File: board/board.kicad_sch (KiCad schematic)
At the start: 4 parts, among them J1 0xx_LED, J2 0xx_LED

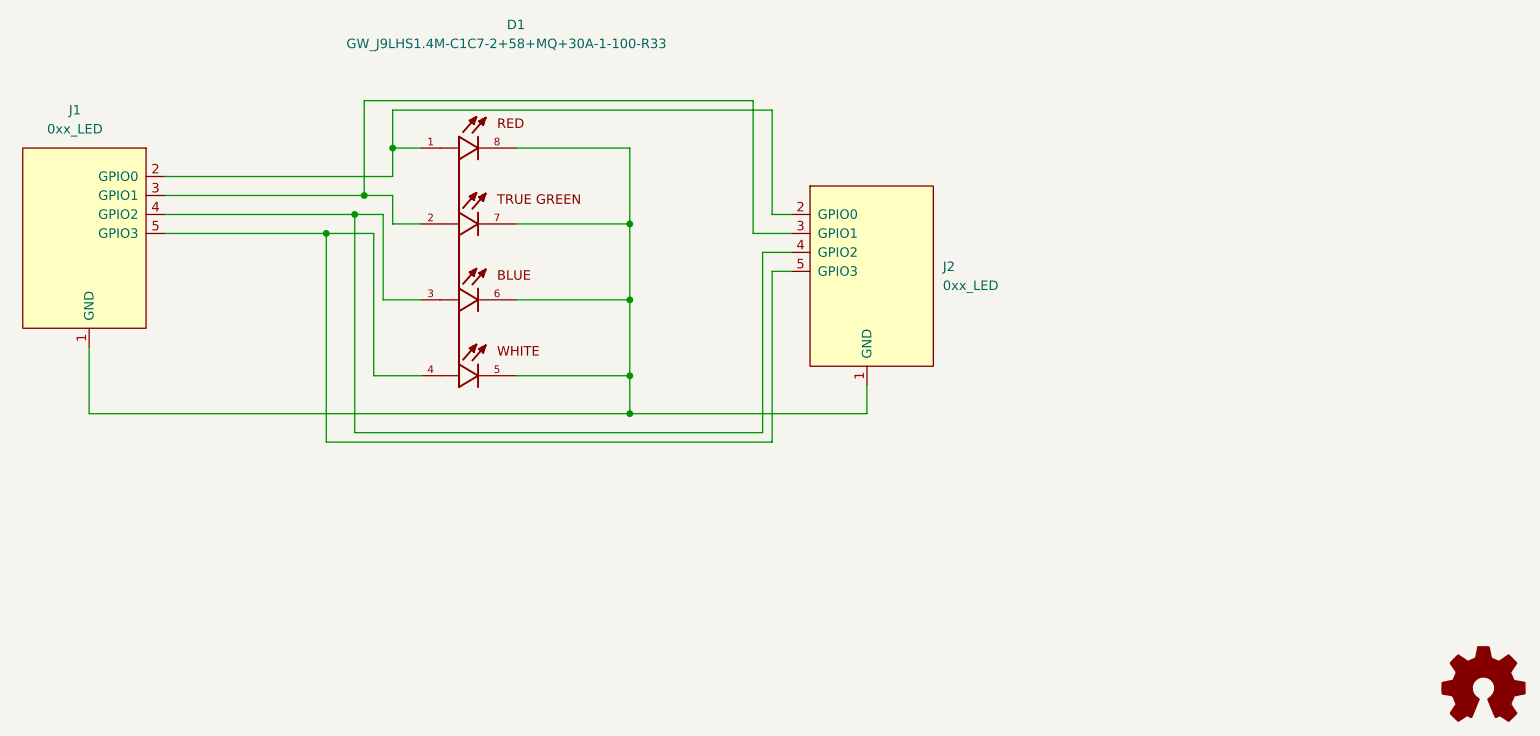
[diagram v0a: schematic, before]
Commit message: Update surface and connected vias | Change common ground to common anode
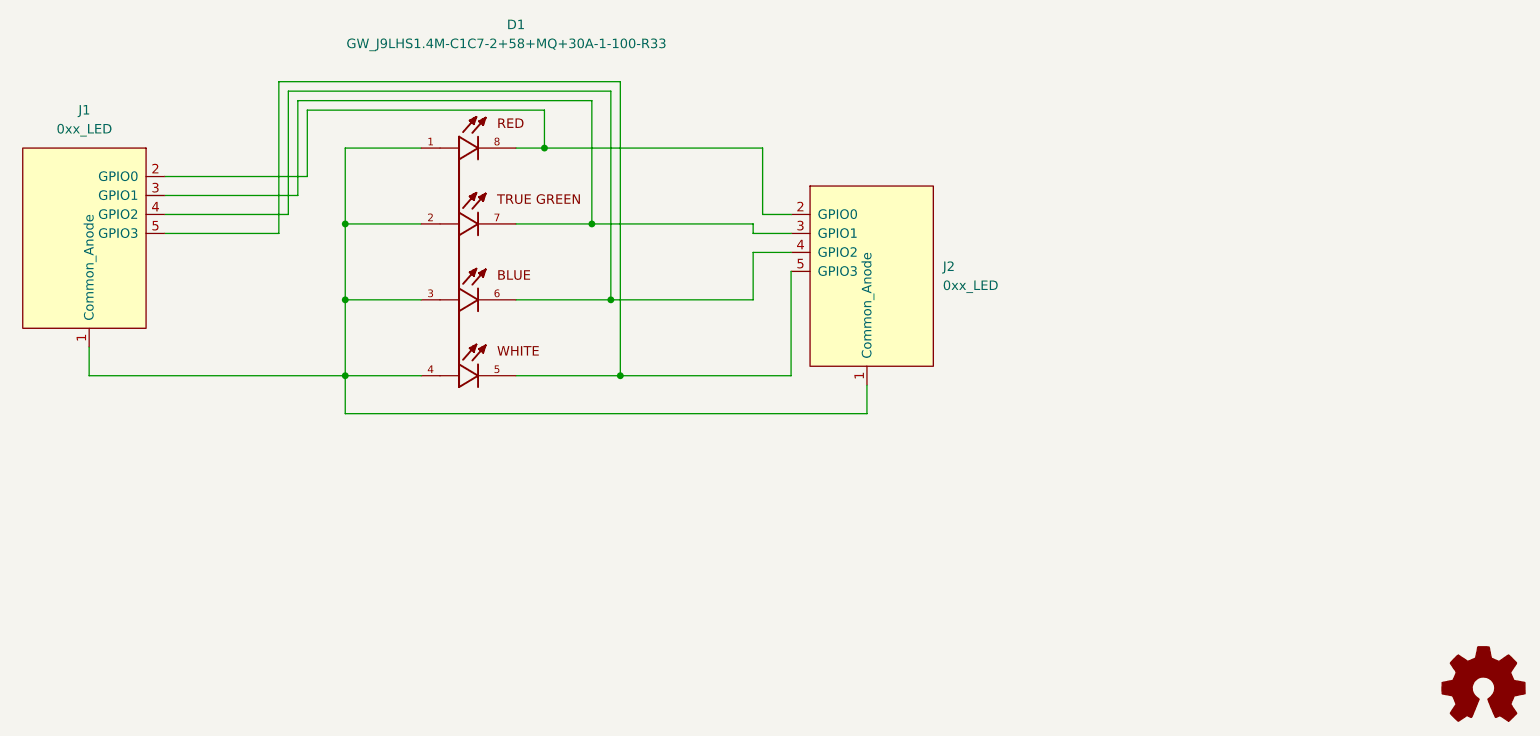
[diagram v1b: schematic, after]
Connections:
- net at J1.2 (GPIO0), J2.2 (GPIO0): now also D1.8; no longer D1.1
- net at J1.3 (GPIO1), J2.3 (GPIO1): now also D1.7; no longer D1.2
- net at J1.4 (GPIO2), J2.4 (GPIO2): now also D1.6; no longer D1.3
- net at J1.5 (GPIO3), J2.5 (GPIO3): now also D1.5; no longer D1.4
- new net: D1.1, D1.2, D1.3, D1.4, J1.1 (Common_Anode), J2.1 (Common_Anode)
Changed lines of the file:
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@@
 (kicad_sch (version 20211123) (generator eeschema)
   (paper "A4")
-  (junction (at 118.11 96.52) (diameter 0) (color 0 0 0 0)
+  (junction (at 120.65 95.25) (diameter 0) (color 0 0 0 0)
   )
-  (junction (at 158.75 95.25) (diameter 0) (color 0 0 0 0)
+  (junction (at 120.65 115.57) (diameter 0) (color 0 0 0 0)
   )
-  (junction (at 127 85.09) (diameter 0) (color 0 0 0 0)
+  (junction (at 156.21 105.41) (diameter 0) (color 0 0 0 0)
   )
-  (junction (at 158.75 105.41) (diameter 0) (color 0 0 0 0)
+  (junction (at 153.67 95.25) (diameter 0) (color 0 0 0 0)
   )
-  (junction (at 158.75 115.57) (diameter 0) (color 0 0 0 0)
+  (junction (at 147.32 85.09) (diameter 0) (color 0 0 0 0)
   )
-  (junction (at 123.19 91.44) (diameter 0) (color 0 0 0 0)
+  (junction (at 120.65 105.41) (diameter 0) (color 0 0 0 0)
   )
-  (junction (at 158.75 120.65) (diameter 0) (color 0 0 0 0)
+  (junction (at 157.48 115.57) (diameter 0) (color 0 0 0 0)
   )
-  (junction (at 121.92 93.98) (diameter 0) (color 0 0 0 0)
-  )
-  (wire (pts (xy 123.19 78.74) (xy 175.26 78.74))
+  (wire (pts (xy 86.36 115.57) (xy 120.65 115.57))
     (stroke (width 0) (type default) (color 0 0 0 0))
   )
-  (wire (pts (xy 123.19 91.44) (xy 127 91.44))
+  (wire (pts (xy 143.51 85.09) (xy 147.32 85.09))
     (stroke (width 0) (type default) (color 0 0 0 0))
   )
-  (wire (pts (xy 127 80.01) (xy 177.8 80.01))
+  (wire (pts (xy 147.32 85.09) (xy 147.32 80.01))
     (stroke (width 0) (type default) (color 0 0 0 0))
   )
-  (wire (pts (xy 118.11 96.52) (xy 96.52 96.52))
-    (stroke (width 0) (type default) (color 0 0 0 0))
-  )
-  (wire (pts (xy 96.52 93.98) (xy 121.92 93.98))
-    (stroke (width 0) (type default) (color 0 0 0 0))
-  )
-  (wire (pts (xy 127 85.09) (xy 127 80.01))
-    (stroke (width 0) (type default) (color 0 0 0 0))
-  )
-  (wire (pts (xy 158.75 95.25) (xy 143.51 95.25))
+  (wire (pts (xy 120.65 105.41) (xy 120.65 115.57))
     (stroke (width 0) (type default) (color 0 0 0 0))
   )
@@
     (stroke (width 0) (type default) (color 0 0 0 0))
   )
-  (wire (pts (xy 175.26 96.52) (xy 180.34 96.52))
+  (wire (pts (xy 153.67 78.74) (xy 153.67 95.25))
     (stroke (width 0) (type default) (color 0 0 0 0))
   )
-  (wire (pts (xy 121.92 123.19) (xy 176.53 123.19))
+  (wire (pts (xy 180.34 96.52) (xy 175.26 96.52))
     (stroke (width 0) (type default) (color 0 0 0 0))
   )
-  (wire (pts (xy 177.8 101.6) (xy 180.34 101.6))
+  (wire (pts (xy 147.32 85.09) (xy 176.53 85.09))
     (stroke (width 0) (type default) (color 0 0 0 0))
   )
-  (wire (pts (xy 158.75 120.65) (xy 86.36 120.65))
+  (wire (pts (xy 180.34 99.06) (xy 175.26 99.06))
     (stroke (width 0) (type default) (color 0 0 0 0))
   )
-  (wire (pts (xy 121.92 93.98) (xy 121.92 123.19))
+  (wire (pts (xy 115.57 88.9) (xy 96.52 88.9))
     (stroke (width 0) (type default) (color 0 0 0 0))
   )
-  (wire (pts (xy 125.73 93.98) (xy 125.73 105.41))
+  (wire (pts (xy 175.26 95.25) (xy 153.67 95.25))
     (stroke (width 0) (type default) (color 0 0 0 0))
   )
-  (wire (pts (xy 127 95.25) (xy 130.81 95.25))
+  (wire (pts (xy 96.52 96.52) (xy 111.76 96.52))
     (stroke (width 0) (type default) (color 0 0 0 0))
   )
-  (wire (pts (xy 127 85.09) (xy 130.81 85.09))
+  (wire (pts (xy 180.34 115.57) (xy 157.48 115.57))
     (stroke (width 0) (type default) (color 0 0 0 0))
   )
-  (wire (pts (xy 123.19 91.44) (xy 123.19 78.74))
+  (wire (pts (xy 120.65 120.65) (xy 190.5 120.65))
     (stroke (width 0) (type default) (color 0 0 0 0))
   )
-  (wire (pts (xy 118.11 124.46) (xy 177.8 124.46))
+  (wire (pts (xy 153.67 95.25) (xy 143.51 95.25))
     (stroke (width 0) (type default) (color 0 0 0 0))
   )
-  (wire (pts (xy 127 88.9) (xy 127 85.09))
+  (wire (pts (xy 130.81 85.09) (xy 120.65 85.09))
     (stroke (width 0) (type default) (color 0 0 0 0))
   )
-  (wire (pts (xy 121.92 93.98) (xy 125.73 93.98))
+  (wire (pts (xy 176.53 93.98) (xy 176.53 85.09))
     (stroke (width 0) (type default) (color 0 0 0 0))
   )
-  (wire (pts (xy 124.46 115.57) (xy 124.46 96.52))
+  (wire (pts (xy 96.52 91.44) (xy 114.3 91.44))
     (stroke (width 0) (type default) (color 0 0 0 0))
   )
-  (wire (pts (xy 158.75 95.25) (xy 158.75 105.41))
+  (wire (pts (xy 180.34 93.98) (xy 176.53 93.98))
     (stroke (width 0) (type default) (color 0 0 0 0))
   )
-  (wire (pts (xy 176.53 99.06) (xy 180.34 99.06))
+  (wire (pts (xy 114.3 78.74) (xy 153.67 78.74))
     (stroke (width 0) (type default) (color 0 0 0 0))
   )
-  (wire (pts (xy 125.73 105.41) (xy 130.81 105.41))
+  (wire (pts (xy 120.65 95.25) (xy 120.65 105.41))
     (stroke (width 0) (type default) (color 0 0 0 0))
   )
-  (wire (pts (xy 177.8 93.98) (xy 180.34 93.98))
+  (wire (pts (xy 175.26 96.52) (xy 175.26 95.25))
     (stroke (width 0) (type default) (color 0 0 0 0))
   )
-  (wire (pts (xy 177.8 80.01) (xy 177.8 93.98))
+  (wire (pts (xy 111.76 76.2) (xy 157.48 76.2))
     (stroke (width 0) (type default) (color 0 0 0 0))
   )
-  (wire (pts (xy 175.26 78.74) (xy 175.26 96.52))
+  (wire (pts (xy 180.34 101.6) (xy 180.34 115.57))
     (stroke (width 0) (type default) (color 0 0 0 0))
   )
-  (wire (pts (xy 130.81 115.57) (xy 124.46 115.57))
+  (wire (pts (xy 86.36 111.76) (xy 86.36 115.57))
     (stroke (width 0) (type default) (color 0 0 0 0))
   )
-  (wire (pts (xy 96.52 88.9) (xy 127 88.9))
+  (wire (pts (xy 157.48 115.57) (xy 143.51 115.57))
     (stroke (width 0) (type default) (color 0 0 0 0))
   )
-  (wire (pts (xy 158.75 105.41) (xy 158.75 115.57))
+  (wire (pts (xy 156.21 105.41) (xy 156.21 77.47))
     (stroke (width 0) (type default) (color 0 0 0 0))
   )
-  (wire (pts (xy 190.5 120.65) (xy 158.75 120.65))
+  (wire (pts (xy 120.65 85.09) (xy 120.65 95.25))
     (stroke (width 0) (type default) (color 0 0 0 0))
   )
-  (wire (pts (xy 127 91.44) (xy 127 95.25))
+  (wire (pts (xy 157.48 76.2) (xy 157.48 115.57))
     (stroke (width 0) (type default) (color 0 0 0 0))
   )
-  (wire (pts (xy 177.8 124.46) (xy 177.8 101.6))
+  (wire (pts (xy 115.57 80.01) (xy 115.57 88.9))
     (stroke (width 0) (type default) (color 0 0 0 0))
   )
-  (wire (pts (xy 143.51 85.09) (xy 158.75 85.09))
+  (wire (pts (xy 147.32 80.01) (xy 115.57 80.01))
     (stroke (width 0) (type default) (color 0 0 0 0))
   )
-  (wire (pts (xy 96.52 91.44) (xy 123.19 91.44))
+  (wire (pts (xy 114.3 91.44) (xy 114.3 78.74))
     (stroke (width 0) (type default) (color 0 0 0 0))
   )
-  (wire (pts (xy 143.51 115.57) (xy 158.75 115.57))
+  (wire (pts (xy 120.65 105.41) (xy 130.81 105.41))
     (stroke (width 0) (type default) (color 0 0 0 0))
   )
-  (wire (pts (xy 158.75 85.09) (xy 158.75 95.25))
+  (wire (pts (xy 143.51 105.41) (xy 156.21 105.41))
     (stroke (width 0) (type default) (color 0 0 0 0))
   )
-  (wire (pts (xy 158.75 105.41) (xy 143.51 105.41))
+  (wire (pts (xy 175.26 99.06) (xy 175.26 105.41))
     (stroke (width 0) (type default) (color 0 0 0 0))
   )
-  (wire (pts (xy 86.36 120.65) (xy 86.36 111.76))
+  (wire (pts (xy 120.65 120.65) (xy 120.65 115.57))
     (stroke (width 0) (type default) (color 0 0 0 0))
   )
-  (wire (pts (xy 176.53 123.19) (xy 176.53 99.06))
+  (wire (pts (xy 156.21 77.47) (xy 113.03 77.47))
     (stroke (width 0) (type default) (color 0 0 0 0))
   )
-  (wire (pts (xy 118.11 96.52) (xy 118.11 124.46))
+  (wire (pts (xy 120.65 95.25) (xy 130.81 95.25))
     (stroke (width 0) (type default) (color 0 0 0 0))
   )
-  (wire (pts (xy 158.75 115.57) (xy 158.75 120.65))
+  (wire (pts (xy 113.03 93.98) (xy 96.52 93.98))
     (stroke (width 0) (type default) (color 0 0 0 0))
   )
-  (wire (pts (xy 124.46 96.52) (xy 118.11 96.52))
+  (wire (pts (xy 111.76 96.52) (xy 111.76 76.2))
+    (stroke (width 0) (type default) (color 0 0 0 0))
+  )
+  (wire (pts (xy 175.26 105.41) (xy 156.21 105.41))
+    (stroke (width 0) (type default) (color 0 0 0 0))
+  )
+  (wire (pts (xy 113.03 77.47) (xy 113.03 93.98))
+    (stroke (width 0) (type default) (color 0 0 0 0))
+  )
+  (wire (pts (xy 120.65 115.57) (xy 130.81 115.57))
     (stroke (width 0) (type default) (color 0 0 0 0))
   )
   (symbol (lib_name "011_GPIO_1") (lib_id "put_on_edge:011_GPIO") (at 85.09 97.79 0) (mirror y) (unit 1)
     (in_bom yes) (on_board yes) (fields_autoplaced)
-    (property "Reference" "J1" (id 0) (at 84.455 80.01 0))
-    (property "Value" "0xx_LED" (id 1) (at 84.455 82.55 0))
-    (property "Footprint" "on_edge:on_edge_2x05_device" (id 2) (at 92.71 81.28 0)
+    (property "Reference" "J1" (id 0) (at 85.725 80.01 0))
+    (property "Value" "0xx_LED" (id 1) (at 85.725 82.55 0))
+    (property "Footprint" "on_edge:on_edge_2x05_device" (id 2) (at 77.47 81.28 0)
       (effects (font (size 1.27 1.27)) hide)
     )
-    (property "Datasheet" "" (id 3) (at 92.71 81.28 0)
+    (property "Datasheet" "" (id 3) (at 77.47 81.28 0)
       (effects (font (size 1.27 1.27)) hide)
     )
